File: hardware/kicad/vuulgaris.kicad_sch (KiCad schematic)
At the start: 177 parts, among them J1 TFPUSH, J10 PJ-603_C41409498, J11 TYPE-C-31-M-12, J2 PJ-376, J3 PJ-376, J4 PJ-376, J5 PJ-376, J7 PJ-603_C41409498, J8 PJ-603_C41409498, J9 PJ-603_C41409498, Q1 J113 / MMBFJ113, Q2 J113 / MMBFJ113, SW1 SW_DPDT_FLAT, SW2 SW_DPDT_FLAT, SW4 CPG151101S03, SW5 CPG151101S03, SW6 CPG151101S03, SW7 CPG151101S03, U1 ES_DAISY_PATCH_SM_REV1, U101 V3205SD, U102 TL072_FLAT, U103 TL072_FLAT, U104 CD4046B, U106 TL072_FLAT, U201 V3205SD, U202 TL072_FLAT, U203 TL072_FLAT, U204 CD4046B, U206 TL072_FLAT, U3 MCP23017-E_SO, U4 MCP23017-E_SO, U5 AMS1117-3.3, U6 AMS1117-3.3, U7 DKM10E-12, U8 78L05

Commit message: hardware: stereo LPG, all eight jacks wired, chip-level pinout audit
Bergman Buchla-style low pass gate, stereo, transcribed as drawn minus CV1 and
the DEEP switch. Four TL074 packages, four VTL5C3 vactrols, hand-built symbols
and footprints for both. Board goes to four layers with a GND plane on In2.Cu.

Six 12mm tactile buttons replace four Cherry MX, 15.5mm column pitch -- the
floor is 14.7mm, where the through-hole pads short.

All eight jacks are wired, which needed both pinouts established first:

  PJ-603 (J7-J10)  2 = sleeve, 4 = tip, 3 = tip normal, 5 = ring
  PJ-376 (J2-J5)   1 = sleeve, 2 = ring, 3 = tip, no switch contact

Both from the manufacturers' drawings. The PJ-603 case is settled by the mono
variant PJ-603-3 keeping 2/3/4 and dropping 5, and corroborated by the footprint
-- pads 3 and 4 share y +2.50 as the switch pair.

Audio in now reaches the Daisy through SW2 SOURCE: jack or resample, one pole
per channel, DC blocking on both legs and a 1M pulldown on each common so the
break-before-make switch cannot leave the input floating mid-throw.

GATE_OUT_2 drives the BBD inhibit on both channels. That cost R28/R29, and
R26/R27 went with them: SLAU550 Rev AB 3.3.3 says the FR26xx boot code does
blank device detection and jumps straight into the BSL when the reset vector
reads 0xFFFF, which "eliminates the need for two additional wires (TEST, RST)".
ADR 0005's hardware entry sequence was never needed, for the first flash either.
Closes Q13 by deletion. Watch the ten-second BSL time-out instead.

Chip-level pinout audit against datasheets, not memory:

- V3205SD hand-built symbol matches the MN3205 block diagram exactly, and the
  VGG divider lands on 4.65V against a spec of 14/15 x VDD = 4.67V
- CD4046, MCP23017 (RESET tied high on both, addresses distinct), TL072/TL074,
  AMS1117, USB-C CC pulldowns, I2C pullups, J12's UART crossing: all correct
- OLED pin 8 FS0 is a FONT CHIP data output, not an interface strap. Left open
  deliberately; pin 9 CS2 he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
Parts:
- removed SW4, SW5, SW6, SW7: CPG151101S03, vuulgaris:KEY-TH_CPG1511F01S0X, symbol vuulgaris:CPG151101S03
- removed U8: 78L05, vuulgaris:SOT-89-3_L4.5-W2.5-P1.50-LS4.2-BR, symbol vuulgaris:78L05_C181132
- added C301, C302, C303, C304, C401, C402, C403, C404: 100nF, vuulgaris:C0603, symbol vuulgaris:C
- added C305, C405: 2nF C0G, vuulgaris:C0603, symbol vuulgaris:C
- added C306, C406, C501, C502, C503, C504: 1uF film, vuulgaris:C0603, symbol vuulgaris:C
- added C307, C407: 220pF C0G, vuulgaris:C0603, symbol vuulgaris:C
- added C308, C408: 4.7nF C0G, vuulgaris:C0603, symbol vuulgaris:C
- added C309, C409: 1nF C0G, vuulgaris:C0603, symbol vuulgaris:C
- added C310, C410: 22pF C0G, vuulgaris:C0603, symbol vuulgaris:C
- added D301, D401: 3V9 zener, vuulgaris:SOD-123_L2.7-W1.6-LS3.7-RD-1, symbol vuulgaris:BZT52C3V9_C2891408
- added J12: FACEPLATE 2x5 IDC, vuulgaris:IDC-TH_10P-P2.54_C5665, symbol vuulgaris:HDR-IDC-2.54-2X5P
- added R303, R403: 150k, vuulgaris:R0603, symbol vuulgaris:R
- added R304, R404: 470k, vuulgaris:R0603, symbol vuulgaris:R
- added R305, R309, R310, R317, R318, R320, R323, R328, R330, R331, R333, R405, R409, R410, R417, R418, R420, R423, R428, R430, R431, R433: 100k, vuulgaris:R0603, symbol vuulgaris:R
- added R306, R406: 470R, vuulgaris:R0603, symbol vuulgaris:R
- added R307, R407: 33k, vuulgaris:R0603, symbol vuulgaris:R
- added R308, R314, R408, R414, R505: 10k, vuulgaris:R0603, symbol vuulgaris:R
- added R311, R411: 15k, vuulgaris:R0603, symbol vuulgaris:R
- added R313, R413: 4M7, vuulgaris:R0603, symbol vuulgaris:R
- added R315, R415, R503, R504: 1k, vuulgaris:R0603, symbol vuulgaris:R
- added R501, R502: 1M, vuulgaris:R0603, symbol vuulgaris:R
- added R506, R507, R508: 47k, vuulgaris:R0603, symbol vuulgaris:R
- added RT301, RT401: 20k trim, vuulgaris:Potentiometer_Bourns_3266W_Vertical, symbol vuulgaris:TRIMPOT_3T
- added SW4, SW5, SW6, SW7, SW8, SW9: 12x12 tactile, vuulgaris:KEY-TH_4P-L12.0-W12.0-P5.00-LS12.5, symbol vuulgaris:TC-1212-7.3-160G
- added U301, U401: TL084, vuulgaris:SOIC-14_3.9x8.7mm_P1.27mm, symbol vuulgaris:TL074_FLAT
- added U302, U402: TL074, vuulgaris:SOIC-14_3.9x8.7mm_P1.27mm, symbol vuulgaris:TL074_FLAT
- added U8: 78L05, vuulgaris:SOT-223-3_L6.5-W3.4-P2.30-LS7.0-BR, symbol vuulgaris:AMS1117-5.0
- added VT301, VT302, VT401, VT402: VTL5C3, vuulgaris:VACTROL-TH_VTL5C3, symbol vuulgaris:VTL5C3
- C42: value 3.3uF -> 10uF
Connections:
- net BBD_INHCV_L is gone; now on net GATE_OUT_2: R117.1
- net BBD_INHCV_R is gone; now on net GATE_OUT_2: R217.1
- net AUDIO_IN_L: now also SW2.2 (A_COM), R501.1
- net AUDIO_IN_R: now also SW2.5 (B_COM), R502.1
- net AUDIO_OUT_L: now also C306.1
- net AUDIO_OUT_R: now also C406.1
- net BBD_IN_L: now also R315.2
- net BBD_IN_R: now also R415.2
- net BBD_OUT_L: now also J9.4, C503.1
- net BBD_OUT_R: now also J10.4, C504.1
- net BTN1: now also SW4.1, SW4.3
- net BTN2: now also SW5.1, SW5.3
- net BTN3: now also SW6.1, SW6.3
- net BTN4: now also SW7.1, SW7.3
- net CV_IN_JACK: now also J4.3
- net GATE_IN: now also J5.3
- net GATE_OUT_1: now also R504.1
- net GND: now also J10.2, J10.5, J2.1, J2.2, J3.1, J3.2, J4.1, J4.2, J5.1, J5.2, J7.2, J7.3, J7.5, J8.2, J8.3, J8.5, J9.2, J9.5, RV1.3, RV1.6, U1.A7 (GND), C301.2, C302.2, C303.2, C304.2, C307.2, C309.2, C401.2, C402.2, C403.2, C404.2, C407.2, C409.2, D301.2 (A), D401.2 (A), J12.10, J12.2, J12.4, J12.6, J12.8, R308.2, R309.2, R310.2, R313.2, R317.2, R318.2, R408.2, R409.2, R410.2, R413.2, R417.2, R418.2, R501.2, R502.2, SW4.2, SW4.4, SW5.2, SW5.4, SW6.2, SW6.4, SW7.2, SW7.4, SW8.2, SW8.4, SW9.2, SW9.4, U302.10 (IN_C+), U302.12 (IN_D+), U302.3 (IN_A+), U302.5 (IN_B+), U402.10 (IN_C+), U402.12 (IN_D+), U402.3 (IN_A+), U402.5 (IN_B+), U8.2 (VOUT), VT302.2 (K), VT402.2 (K)
- net LPG_ENV: now also RV3.1, RV3.4, R323.1, R423.1, R503.1
- net MSP430_RXD: now also J12.5
- net MSP430_TXD: now also J12.3
- net NEG12V: now also C302.1, C304.1, C402.1, C404.1, U301.11 (V-), U302.11 (V-), U401.11 (V-), U402.11 (V-)
- net OLED_RES: now also U1.A9 (USB_DP)
- net P3V3_DAISY: now also R506.2, R507.2, R508.2
- net P3V3_MSP430: now also J12.1
- net P3V3_OLED: now also R505.2
- net P5V_BBD: now also U8.1 (GND)
- net POS12V: now also RV1.1, RV1.4, C301.1, C303.1, C401.1, C403.1, U301.4 (V+), U302.4 (V+), U401.4 (V+), U402.4 (V+), U8.3 (VIN)
- net SD_CMD: now also R506.1
- net SD_D0: now also R507.1
- net LPG_RES_L: now reaches RV2.1
- net LPG_RES_L: now also SW1.1 (A_NC), C310.2, U301.14 (OUT_D)
- net LPG_RESW_L: now reaches RV2.2
- net LPG_RESW_L: now also C310.1, U301.13 (IN_D-)
- net LPG_RESL_L: now reaches RV2.3
- net LPG_RESL_L: now also R318.1
- net LPG_RES_R: now reaches RV2.4
- net LPG_RES_R: now also SW1.4 (B_NC), C410.2, U401.14 (OUT_D)
- net LPG_RESW_R: now reaches RV2.5
- net LPG_RESW_R: now also C410.1, U401.13 (IN_D-)
- net LPG_RESL_R: now reaches RV2.6
- net LPG_RESL_R: now also R418.1
- net LPG_VCFSW_L: now reaches SW1.2 (A_COM)
- net LPG_VCFSW_L: now also C308.2
- net LPG_VCFSW_R: now reaches SW1.5 (B_COM)
- net LPG_VCFSW_R: now also C408.2
- net SRC_EXT_L: now reaches SW2.1 (A_NC)
- net SRC_EXT_L: now also C501.2
- net SRC_RSMP_L: now reaches SW2.3 (A_NO)
- net SRC_RSMP_L: now also C503.2
- net SRC_EXT_R: now reaches SW2.4 (B_NC)
- net SRC_EXT_R: now also C502.2
- net SRC_RSMP_R: now reaches SW2.6 (B_NO)
- net SRC_RSMP_R: now also C504.2
- net OLED_FONTCS: now reaches DS1.9 (CS2)
- net OLED_FONTCS: now also R505.1
- net SD_DAT3: now reaches J1.2 (CD/DAT3)
- net SD_DAT3: now also R508.1
- net EXT_IN_L: now reaches J7.4
- net EXT_IN_L: now also C501.1
- net CVOUT_JACK: now reaches J2.3
- net CVOUT_JACK: now also R503.2
- net EXT_IN_R: now reaches J8.4
- net EXT_IN_R: now also C502.1
- net LPG_OFS_L: now reaches RV1.2
- net LPG_OFS_L: now also R303.1
- net LPG_OFS_R: now reaches RV1.5
- net LPG_OFS_R: now also R403.1
- net BTN5: now reaches U4.21 (GPA0)
- net BTN5: now also SW8.1, SW8.3
- net BTN6: now reaches U4.22 (GPA1)
- net BTN6: now also SW9.1, SW9.3
- net GATEOUT_JACK: now reaches J3.3
- net GATEOUT_JACK: now also R504.2
- net LPG_CVW_L: now reaches RV3.2
- net LPG_CVW_L: now also R328.1
- net LPG_ENVN_L: now reaches RV3.3
- net LPG_ENVN_L: now also R320.2, U302.1 (OUT_A)
- net LPG_CVW_R: now reaches RV3.5
- net LPG_CVW_R: now also R428.1
- net LPG_ENVN_R: now reaches RV3.6
- net LPG_ENVN_R: now also R420.2, U402.1 (OUT_A)
- new net LPG_ABUF_L: R311.1, U301.1 (OUT_A), VT301.3 (CELL1)
- new net LPG_ABUF_R: R411.1, U401.1 (OUT_A), VT401.3 (CELL1)
- new net LPG_AFB_L: R311.2, U301.2 (IN_A-)
- new net LPG_AFB_R: R411.2, U401.2 (IN_A-)
- new net LPG_BOUT_L: R306.1, U301.7 (OUT_B)
- new net LPG_BOUT_R: R406.1, U401.7 (OUT_B)
- new net LPG_BP_L: R308.1, U301.5 (IN_B+)
- new net LPG_BP_R: R408.1, U401.5 (IN_B+)
- new net LPG_C5_L: C305.2, R304.1
- new net LPG_C5_R: C405.2, R404.1
- new net LPG_CFB_L: R314.1, U301.9 (IN_C-)
- new net LPG_CFB_R: R414.1, U401.9 (IN_C-)
- new net LPG_CVC_L: R331.2, R333.1, U302.9 (IN_C-)
- new net LPG_CVC_R: R431.2, R433.1, U402.9 (IN_C-)
- new net LPG_CVD_L: R330.2, R331.1, U302.14 (OUT_D)
- new net LPG_CVD_R: R430.2, R431.1, U402.14 (OUT_D)
- new net LPG_CVI_L: R320.1, R323.2, U302.2 (IN_A-)
- new net LPG_CVI_R: R420.1, R423.2, U402.2 (IN_A-)
- new net LPG_CV_L: R304.2, R305.2, R333.2, U302.8 (OUT_C)
- new net LPG_CV_R: R404.2, R405.2, R433.2, U402.8 (OUT_C)
- new net LPG_INF_L: C306.2, R309.1, R310.1, U301.3 (IN_A+)
- new net LPG_INF_R: C406.2, R409.1, R410.1, U401.3 (IN_A+)
- new net LPG_LDR_L: C309.1, R313.1, U301.10 (IN_C+), VT302.4 (CELL2)
- new net LPG_LDR_R: C409.1, R413.1, U401.10 (IN_C+), VT402.4 (CELL2)
- new net LPG_LEDM_L: VT301.2 (K), VT302.1 (A)
- new net LPG_LEDM_R: VT401.2 (K), VT402.1 (A)
- new net LPG_LED_L: D301.1 (C), R306.2, R307.2, R317.1, VT301.1 (A)
- new net LPG_LED_R: D401.1 (C), R406.2, R407.2, R417.1, VT401.1 (A)
- new net LPG_MID_L: C307.1, C308.1, VT301.4 (CELL2), VT302.3 (CELL1)
- new net LPG_MID_R: C407.1, C408.1, VT401.4 (CELL2), VT402.3 (CELL1)
- new net LPG_NC_L: U302.6 (IN_B-), U302.7 (OUT_B)
- new net LPG_NC_R: U402.6 (IN_B-), U402.7 (OUT_B)
- new net LPG_OUT_L: R314.2, R315.1, U301.12 (IN_D+), U301.8 (OUT_C)
- new net LPG_OUT_R: R414.2, R415.1, U401.12 (IN_D+), U401.8 (OUT_C)
- new net LPG_SUMCV_L: R328.2, R330.1, U302.13 (IN_D-)
- new net LPG_SUMCV_R: R428.2, R430.1, U402.13 (IN_D-)
- new net LPG_SUM_L: C305.1, R303.2, R305.1, RT301.1, U301.6 (IN_B-)
- new net LPG_SUM_R: C405.1, R403.2, R405.1, RT401.1, U401.6 (IN_B-)
- new net LPG_T1_L: R307.1, RT301.2 (WIPER), RT301.3
- new net LPG_T1_R: R407.1, RT401.2 (WIPER), RT401.3
- new net MSP_RST: J12.7
- new net MSP_TEST: J12.9
- no-connect marks 142 -> 83

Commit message: hardware: ground all 30 chassis lugs
ENC0 pins 6/7, ENC1-ENC8 D/E, RV1-RV6 7/8 -- the mounting tabs, which in each
footprint are the large slotted ovals set apart from the signal pads. On the
EC11 it is 6/7 rather than D/E, since D/E there are the push switch.

Grounded rather than left open: this instrument reads capacitance and a floating
metal shell right behind the touch panel is an antenna. The joints also take
mechanical load off the signal pins.

848/848 connections verified, 0 unintended. Floating pins 83 -> 53.
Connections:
- net GND: now also ENC0.6 (EH), ENC0.7 (EH), ENC1.D, ENC1.E, ENC2.D, ENC2.E, ENC3.D, ENC3.E, ENC4.D, ENC4.E, ENC5.D, ENC5.E, ENC6.D, ENC6.E, ENC7.D, ENC7.E, ENC8.D, ENC8.E, RV1.7, RV1.8, RV2.7, RV2.8, RV3.7, RV3.8, RV4.7, RV4.8, RV5.7, RV5.8, RV6.7, RV6.8
- no-connect marks 83 -> 53

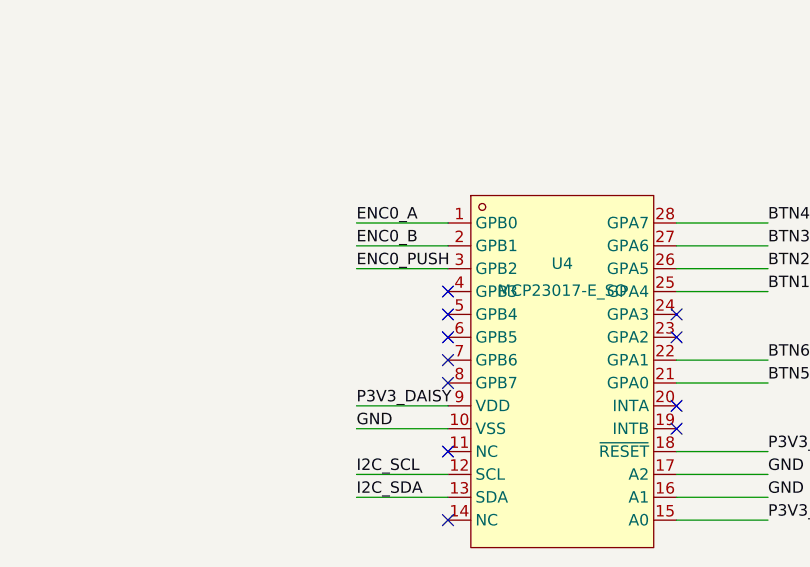
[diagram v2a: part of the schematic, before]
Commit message: hardware: MSP430 reset on U4 GPB3, across J12.7
Nothing drove MSP_RST after R26-R29 came out -- the ribbon conductor existed but
connected to nothing on this board, so a main-board-driven reset was impossible.

On a spare expander GPIO rather than a Daisy pin: every Daisy candidate is spoken
for (B5 gate out jack, B6 BBD inhibit, A9 OLED reset, A8 reserved), U4 uses 9 of
16, and the MCP23017 runs on 3V3 against an MSP430 max of 3.6V -- a direct wire
with no divider, which is the thing Q13 warned about. On I2C rather than the
UART, so it works when the touch chip is too wedged to answer on the serial link.

Not for BSL; blank detection covers that. This is a recovery reset, and a way to
re-arm the BSL after the ten-second time-out without power-cycling.

MCP23017 GPIO power up high-Z, so the pullup and cap TI specifies on RST/NMI are
now required on the faceplate, not merely good practice.

849/849 connections verified, 0 unintended.
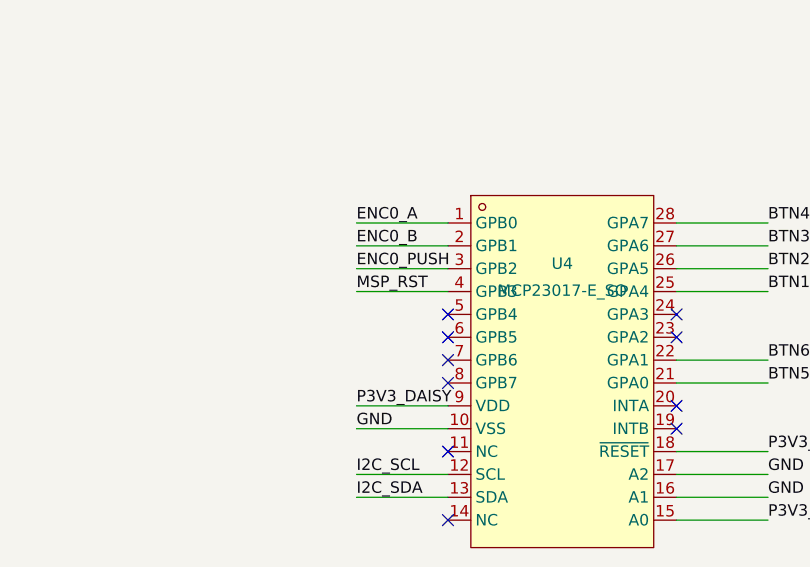
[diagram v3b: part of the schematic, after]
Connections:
- net MSP_RST: now also U4.4 (GPB3)
- no-connect marks 53 -> 52
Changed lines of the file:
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@@
   (wire (pts (xy 352.7 236.27) (xy 362.86 236.27)) (stroke (width 0) (type solid)))
   (wire (pts (xy 352.7 233.73) (xy 362.86 233.73)) (stroke (width 0) (type solid)))
+  (wire (pts (xy 327.3 226.11) (xy 317.14 226.11)) (stroke (width 0) (type solid)))
   (wire (pts (xy 104.76 4007.3) (xy 94.6 4007.3)) (stroke (width 0) (type solid)))
   (wire (pts (xy 104.76 4004.76) (xy 94.6 4004.76)) (stroke (width 0) (type solid)))
@@
     (effects (font (size 1.27 1.27)) (justify left bottom))
   )
+  (label "MSP_RST" (at 317.14 226.11 180) (fields_autoplaced)
+    (effects (font (size 1.27 1.27)) (justify left bottom))
+  )
   (label "LPG_INF_R" (at 94.6 4007.3 180) (fields_autoplaced)
     (effects (font (size 1.27 1.27)) (justify left bottom))
@@
   (no_connect (at 352.7 101.35))
   (no_connect (at 352.7 98.81))
-  (no_connect (at 327.3 226.11))
   (no_connect (at 327.3 228.65))
   (no_connect (at 327.3 231.19))
